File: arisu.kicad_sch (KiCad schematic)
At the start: 40 parts, among them J1 USB_B_Micro, J10 PF6, J11 PF7, J12 VCC, J13 D+, J14 D-, J15 GND, J2 MISO, J3 VCC, J4 SCK, J5 MOSI, J6 RES, J7 GND, J8 PF4, J9 PF5, U1 USBLC6-2SC6, U2 ATmega32U4-AU, Y1 Crystal_GND24

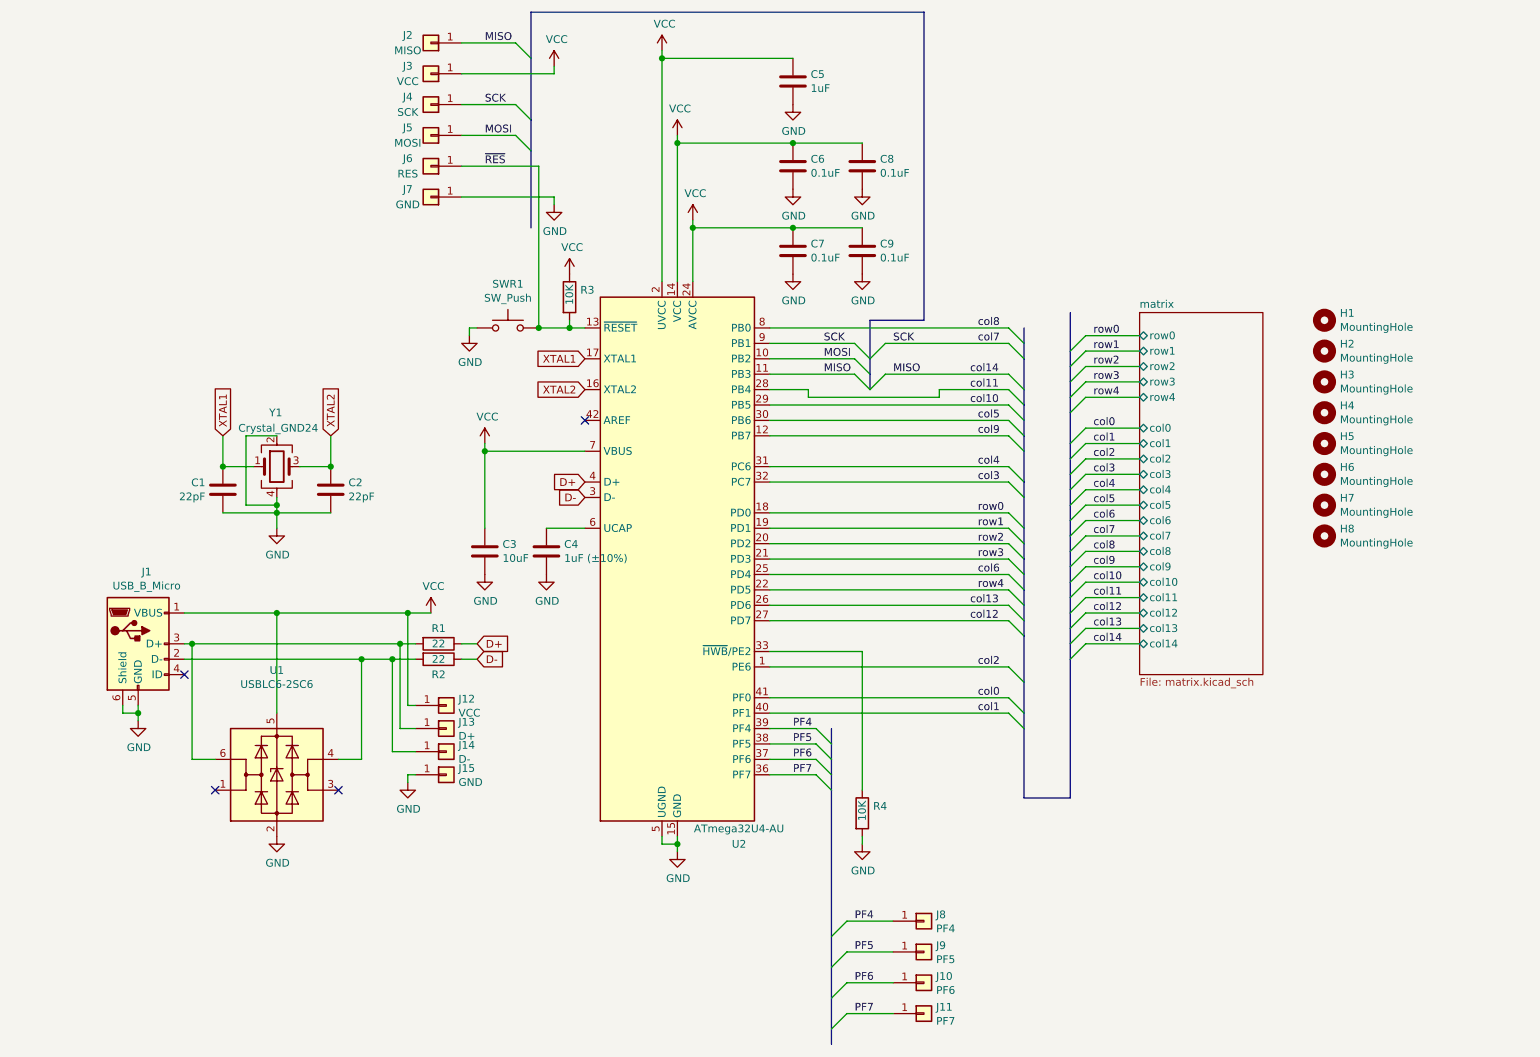
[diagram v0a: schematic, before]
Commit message: Change USB port, add DB conn, add some keys
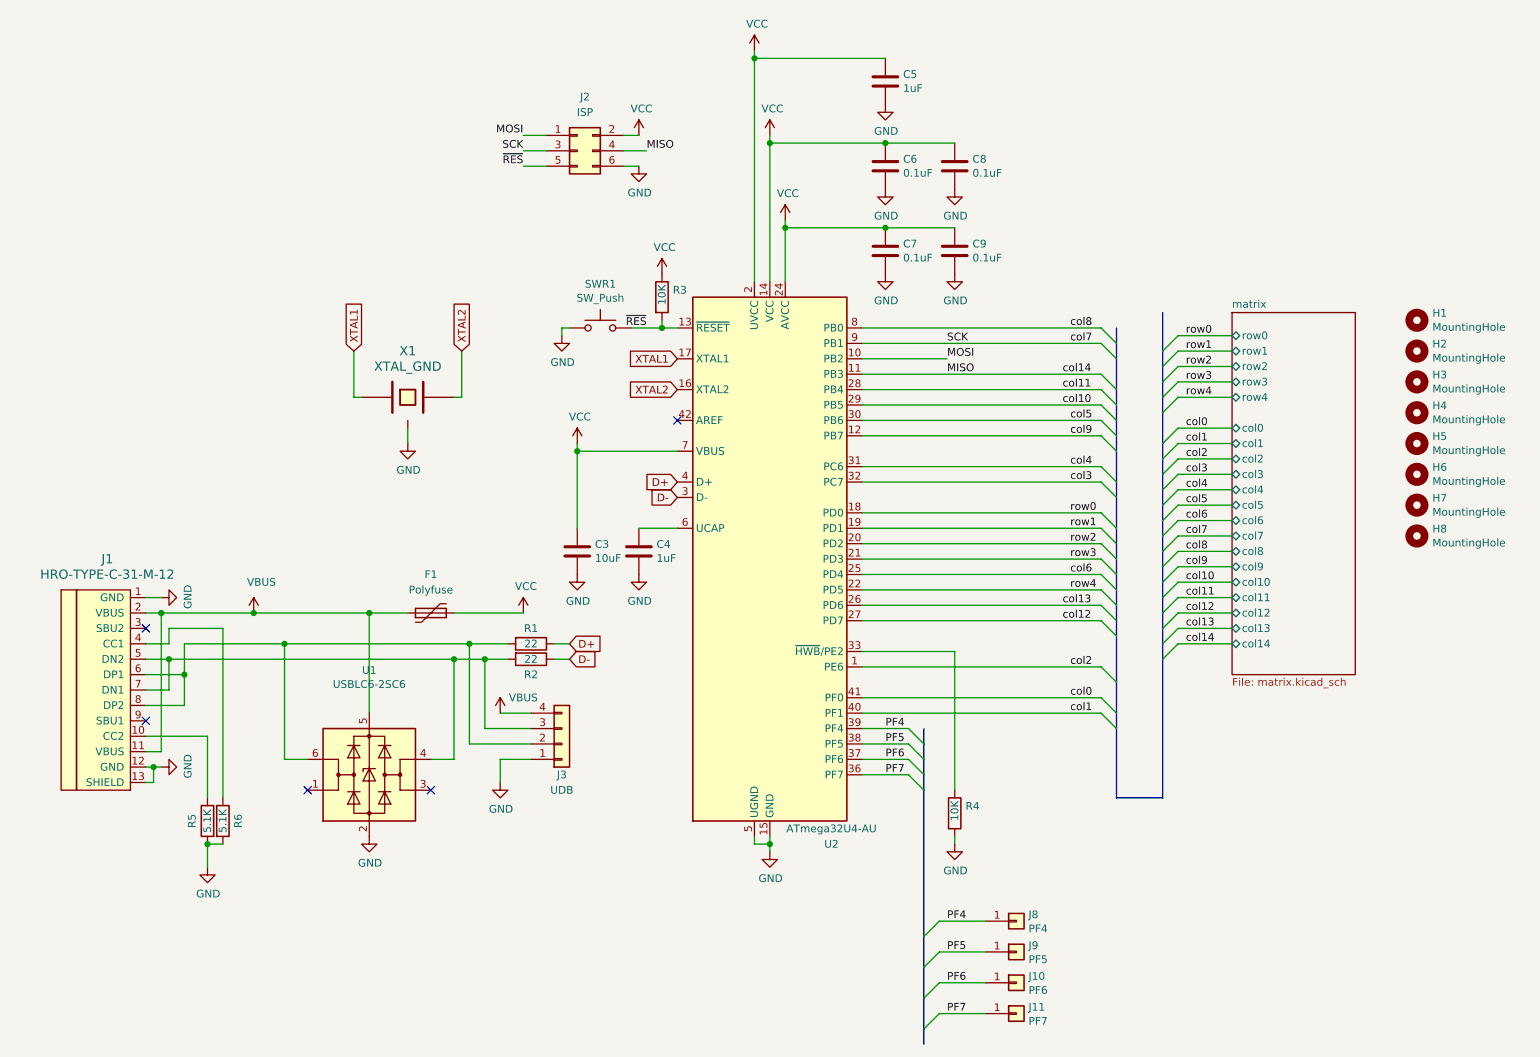
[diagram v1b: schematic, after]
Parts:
- removed C1, C2: 22pF, Capacitors_SMD:C_0805_HandSoldering, symbol Device:C
- removed J1: USB_B_Micro, Connectors_USB:USB_Micro-B_Molex-105017-0001, symbol arisu-rescue:USB_B_Micro-Connector
- removed J12, J3: VCC, Pin_Headers:Pin_Header_Straight_1x01_Pitch2.54mm, symbol Connector_Generic:Conn_01x01
- removed J13: D+, Pin_Headers:Pin_Header_Straight_1x01_Pitch2.54mm, symbol Connector_Generic:Conn_01x01
- removed J14: D-, Pin_Headers:Pin_Header_Straight_1x01_Pitch2.54mm, symbol Connector_Generic:Conn_01x01
- removed J15, J7: GND, Pin_Headers:Pin_Header_Straight_1x01_Pitch2.54mm, symbol Connector_Generic:Conn_01x01
- removed J2: MISO, Pin_Headers:Pin_Header_Straight_1x01_Pitch2.54mm, symbol Connector_Generic:Conn_01x01
- removed J4: SCK, Pin_Headers:Pin_Header_Straight_1x01_Pitch2.54mm, symbol Connector_Generic:Conn_01x01
- removed J5: MOSI, Pin_Headers:Pin_Header_Straight_1x01_Pitch2.54mm, symbol Connector_Generic:Conn_01x01
- removed J6: RES, Pin_Headers:Pin_Header_Straight_1x01_Pitch2.54mm, symbol Connector_Generic:Conn_01x01
- removed Y1: Crystal_GND24, Crystals:Crystal_SMD_SeikoEpson_FA238-4pin_3.2x2.5mm_HandSoldering, symbol Device:Crystal_GND24
- added F1: Polyfuse, Keeb_components:R_0805, symbol Device:Polyfuse
- added J1: HRO-TYPE-C-31-M-12, Keeb_components:HRO-TYPE-C-31-M-12, symbol Type-C:HRO-TYPE-C-31-M-12
- added J2: ISP, Keeb_components:isp_standard, symbol Connector_Generic:Conn_02x03_Odd_Even
- added J3: UDB, Keeb_components:JST_SH_SM04B-SRSS-TB_1x04-1MP_P1.00mm_Horizontal, symbol Connector_Generic:Conn_01x04
- added R5, R6: 5.1K, Keeb_components:R_0805, symbol Device:R
- added X1: XTAL_GND, Keeb_components:Resonator_SMD_muRata_CSTNExxV-3Pin-p1.2, symbol keyboard_parts:XTAL_GND
- C3, C5, C6, C7, C8, C9: footprint Capacitors_SMD:C_0805_HandSoldering -> Keeb_components:C_0805
- C4: value 1uF (±10%) -> 1uF; footprint Capacitors_SMD:C_0805_HandSoldering -> Keeb_components:C_0805
- R1, R2, R3, R4: footprint Resistors_SMD:R_0805_HandSoldering -> Keeb_components:R_0805
- U1: footprint TO_SOT_Packages_SMD:SOT-23-6_Handsoldering -> Keeb_components:USBLC6-2SC6
- U2: footprint Housings_QFP:TQFP-44_10x10mm_Pitch0.8mm -> Keeb_components:ATMEGA32U4
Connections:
- net GND: now also J1.1 (GND), J1.12 (GND), J1.13 (SHIELD), J2.6 (Pin_6), J3.1 (Pin_1), R5.2, R6.2, X1.3
- net MISO: now also J2.4 (Pin_4)
- net MOSI: now also J2.1 (Pin_1)
- net SCK: now also J2.3 (Pin_3)
- net VCC: now also F1.2, J2.2 (Pin_2); no longer U1.5 (VBUS)
- net XTAL1: now also X1.1
- net XTAL2: now also X1.2
- net ~RES~: now also J2.5 (Pin_5)
- net at R2.2, U1.4 (I/O2): now also J1.5 (DN2), J1.7 (DN1), J3.3 (Pin_3)
- net at R1.2, U1.6 (I/O1): now also J1.6 (DP1), J1.8 (DP2), J3.2 (Pin_2)
- new net: J1.10 (CC2), R5.1
- new net: J1.4 (CC1), R6.1
- new net VBUS: F1.1, J1.11 (VBUS), J1.2 (VBUS), J3.4 (Pin_4), U1.5 (VBUS)
- no-connect marks 4 -> 5
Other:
- moved on the sheet: C3, C4, C5, C6, C7, C8, C9, H1, H2, H3, H4, H5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
